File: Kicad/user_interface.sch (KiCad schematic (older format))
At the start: 33 parts, among them SW1 Push, SW10 Push, SW11 Push, SW12 Push, SW13 Rotary_Encoder_Switch, SW14 Rotary_Encoder_Switch, SW15 Rotary_Encoder_Switch, SW2 Push, SW3 Push, SW4 Push, SW5 Push, SW6 Push, SW7 Push, SW8 Push, SW9 Push, U1 TLC59281DBQ

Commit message: completing schematics and starting to correct errors
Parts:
- gave numbers to parts that had none: 17
- renumbered U1 to U3
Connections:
- net GND: now also SW13.C, SW14.C, SW15.C

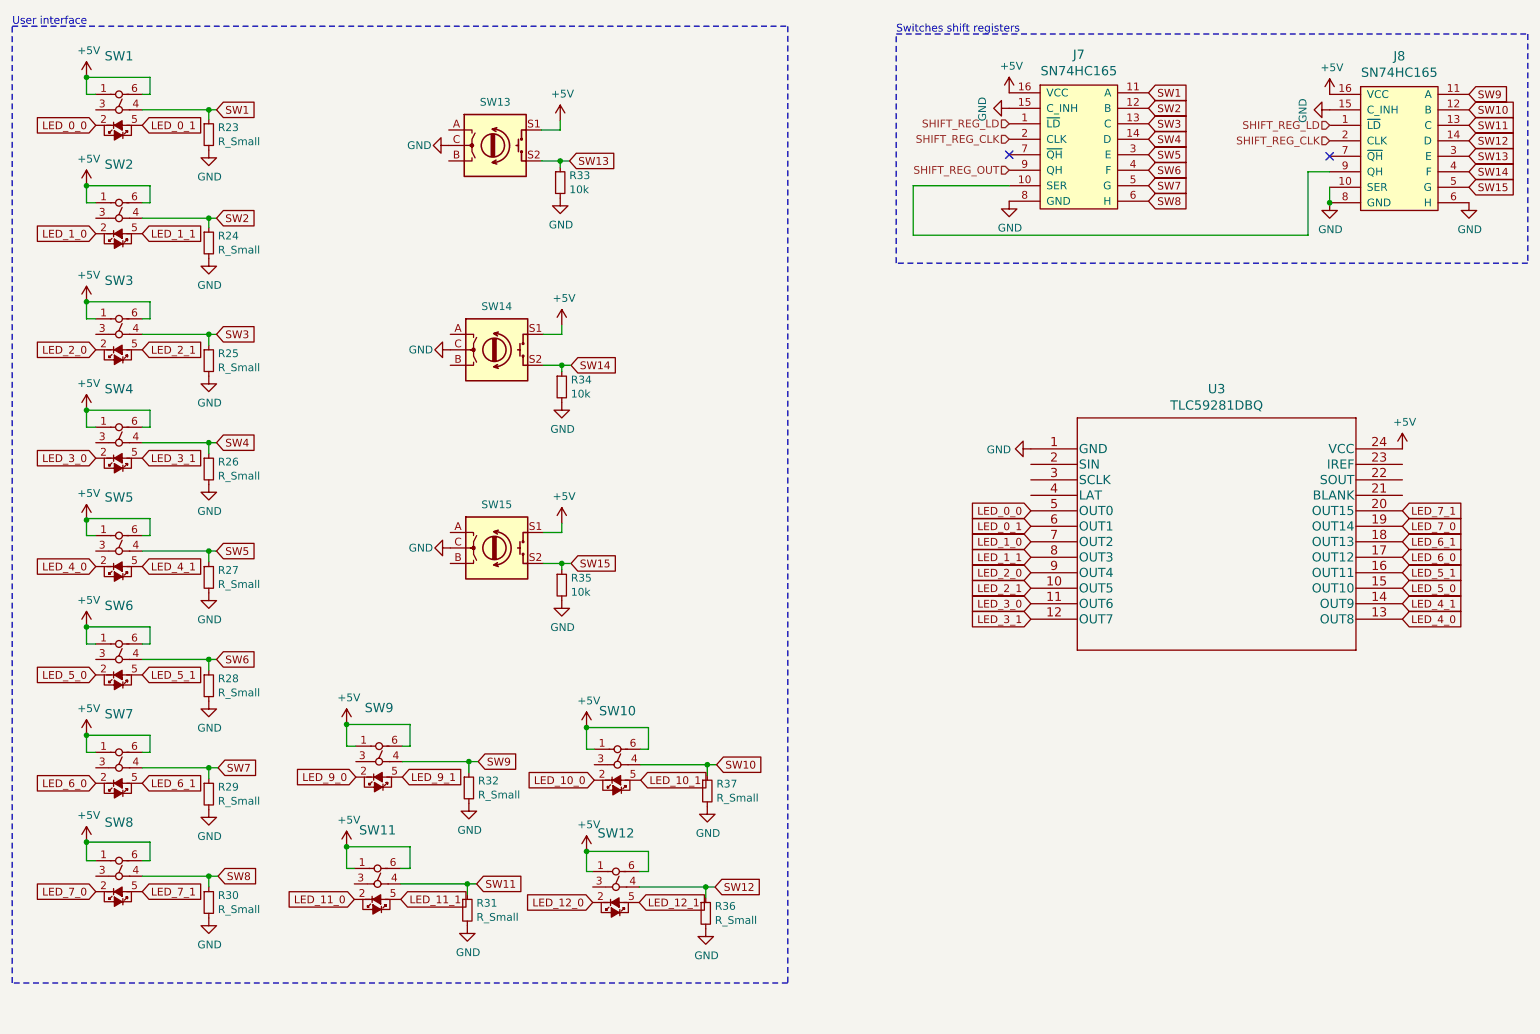
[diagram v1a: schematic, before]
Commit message: correcting some connections
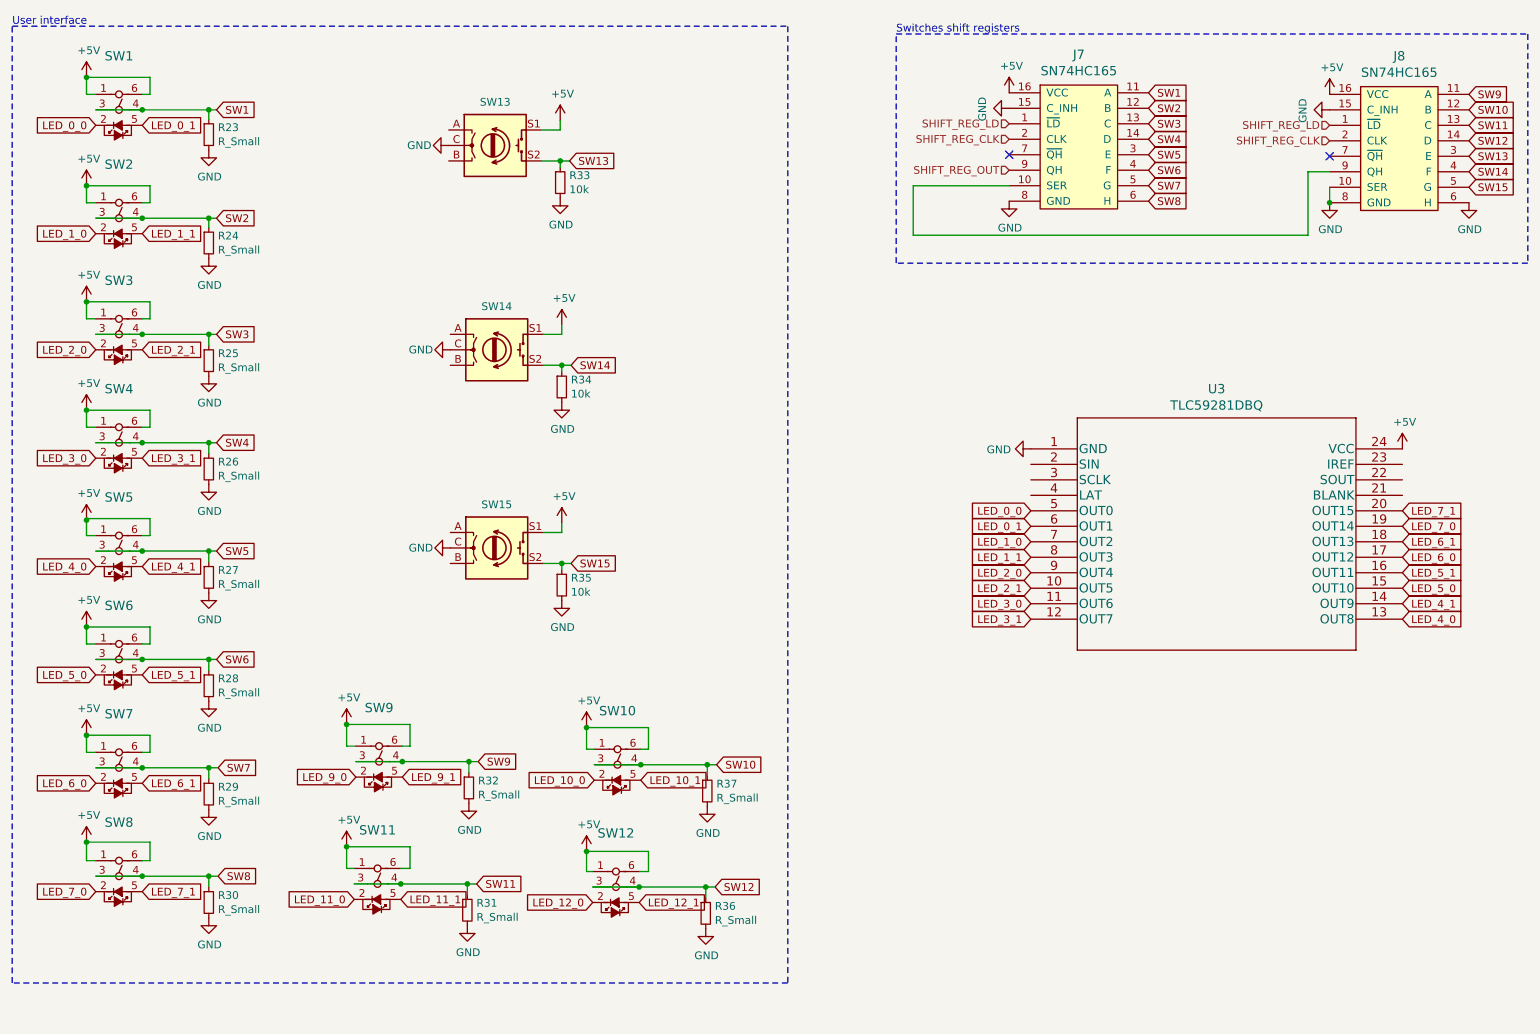
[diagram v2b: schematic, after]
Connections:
- net SW1: now also SW1.3
- net SW10: now also SW10.3
- net SW11: now also SW11.3
- net SW12: now also SW12.3
- net SW2: now also SW2.3
- net SW3: now also SW3.3
- net SW4: now also SW4.3
- net SW5: now also SW5.3
- net SW6: now also SW6.3
- net SW7: now also SW7.3
- net SW8: now also SW8.3
- net SW9: now also SW9.3
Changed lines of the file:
@@
 	0    1    1    0
 $EndComp
+Wire Wire Line
+	1550 1450 1850 1450
+Connection ~ 1850 1450
+Wire Wire Line
+	1550 2150 1850 2150
+Connection ~ 1850 2150
+Wire Wire Line
+	1550 2900 1850 2900
+Connection ~ 1850 2900
+Wire Wire Line
+	1550 3600 1850 3600
+Connection ~ 1850 3600
+Wire Wire Line
+	1550 4300 1850 4300
+Connection ~ 1850 4300
+Wire Wire Line
+	1550 5000 1850 5000
+Connection ~ 1850 5000
+Wire Wire Line
+	1550 5700 1850 5700
+Connection ~ 1850 5700
+Wire Wire Line
+	1550 6400 1850 6400
+Connection ~ 1850 6400
+Wire Wire Line
+	3230 5660 3530 5660
+Connection ~ 3530 5660
+Wire Wire Line
+	3220 6450 3520 6450
+Connection ~ 3520 6450
+Wire Wire Line
+	4770 5680 5070 5680
+Connection ~ 5070 5680
+Wire Wire Line
+	4760 6470 5060 6470
+Connection ~ 5060 6470
 $EndSCHEMATC

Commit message: updated power section with switching regulator
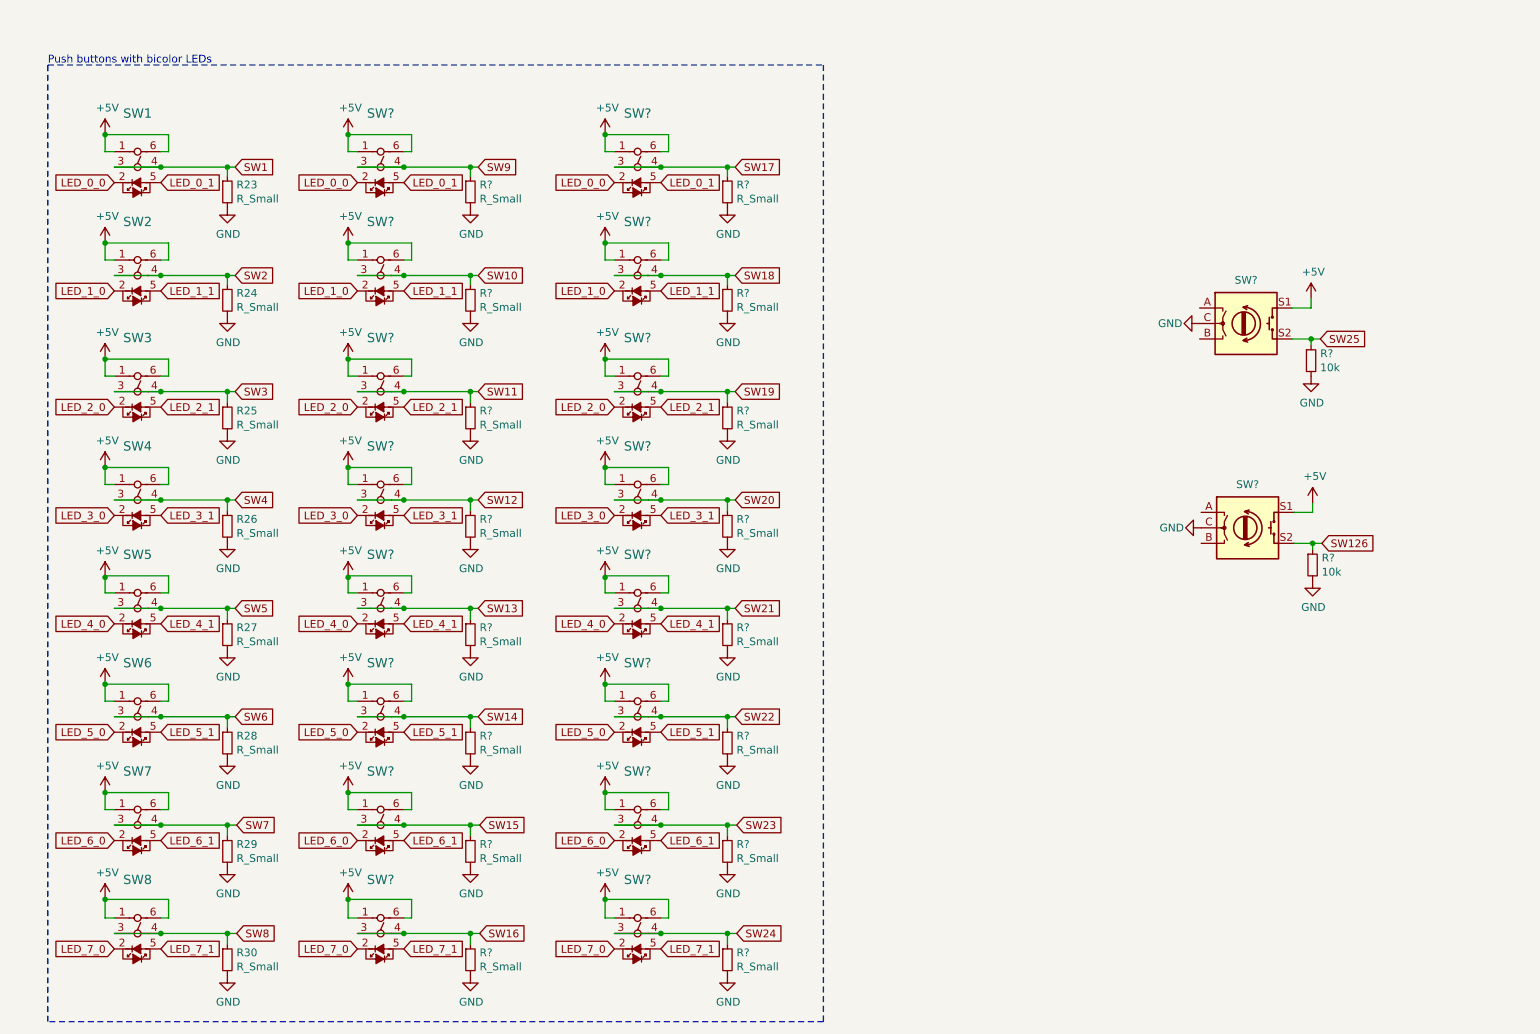
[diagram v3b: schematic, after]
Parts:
- removed J7, J8: SN74HC165, symbol eurocad:SN74HC165
- removed R31, R32, R36, R37: R_Small, symbol Device:R_Small
- removed R33, R34, R35: 10k, symbol Device:R_Small
- removed SW10, SW11, SW12, SW9: Push, footprints:PB614_LED_SW_6pin, symbol sw_push_led_pb614:SW_Push_LED_PB614
- removed SW13, SW14, SW15: Rotary_Encoder_Switch, Rotary_Encoder:RotaryEncoder_Alps_EC12E-Switch_Vertical_H20mm, symbol Device:Rotary_Encoder_Switch
- removed U3: TLC59281DBQ, Package_DFN_QFN:VQFN-24-1EP_4x4mm_P0.5mm_EP2.45x2.45mm, symbol eurorack_custom:ul_TLC59281DBQ_TLC59281DBQ
- added R? (x16): R_Small, symbol Device:R_Small
- added R? (x2): 10k, symbol Device:R_Small
- added SW? (x16): Push, footprints:PB614_LED_SW_6pin, symbol sw_push_led_pb614:SW_Push_LED_PB614
- added SW? (x2): Rotary_Encoder_Switch, Rotary_Encoder:RotaryEncoder_Alps_EC12E-Switch_Vertical_H20mm, symbol Device:Rotary_Encoder_Switch
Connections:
- net +5V: now also SW?.1, SW?.1, SW?.1, SW?.1, SW?.1, SW?.1, SW?.1, SW?.1, SW?.1, SW?.1, SW?.1, SW?.1, SW?.1, SW?.1, SW?.1, SW?.1, SW?.6, SW?.6, SW?.6, SW?.6, SW?.6, SW?.6, SW?.6, SW?.6, SW?.6, SW?.6, SW?.6, SW?.6, SW?.6, SW?.6, SW?.6, SW?.6, SW?.S1, SW?.S1
- net GND: now also R?.2, R?.2, R?.2, R?.2, R?.2, R?.2, R?.2, R?.2, R?.2, R?.2, R?.2, R?.2, R?.2, R?.2, R?.2, R?.2, R?.2, R?.2, SW?.C, SW?.C
- net LED_0_0: now also SW?.2, SW?.2
- net LED_0_1: now also SW?.5, SW?.5
- net LED_1_0: now also SW?.2, SW?.2
- net LED_1_1: now also SW?.5, SW?.5
- net LED_2_0: now also SW?.2, SW?.2
- net LED_2_1: now also SW?.5, SW?.5
- net LED_3_0: now also SW?.2, SW?.2
- net LED_3_1: now also SW?.5, SW?.5
- net LED_4_0: now also SW?.2, SW?.2
- net LED_4_1: now also SW?.5, SW?.5
- net LED_5_0: now also SW?.2, SW?.2
- net LED_5_1: now also SW?.5, SW?.5
- net LED_6_0: now also SW?.2, SW?.2
- net LED_6_1: now also SW?.5, SW?.5
- net LED_7_0: now also SW?.2, SW?.2
- net LED_7_1: now also SW?.5, SW?.5
- net SW10: now also R?.1, SW?.3, SW?.4
- net SW11: now also R?.1, SW?.3, SW?.4
- net SW12: now also R?.1, SW?.3, SW?.4
- net SW13: now also R?.1, SW?.3, SW?.4
- net SW14: now also R?.1, SW?.3, SW?.4
- net SW15: now also R?.1, SW?.3, SW?.4
- net SW9: now also R?.1, SW?.3, SW?.4
- new net SW126: R?.1, SW?.S2
- new net SW16: R?.1, SW?.3, SW?.4
- new net SW17: R?.1, SW?.3, SW?.4
- new net SW18: R?.1, SW?.3, SW?.4
- new net SW19: R?.1, SW?.3, SW?.4
- new net SW20: R?.1, SW?.3, SW?.4
- new net SW21: R?.1, SW?.3, SW?.4
- new net SW22: R?.1, SW?.3, SW?.4
- new net SW23: R?.1, SW?.3, SW?.4
- new net SW24: R?.1, SW?.3, SW?.4
- new net SW25: R?.1, SW?.S2
- no-connect marks 2 -> 0
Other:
- note added: "Push buttons with bicolor LEDs"
- note removed: "Switches shift registers"
- note removed: "User interface"
- moved on the sheet: R23, R24, R25, R26, R27, R28, R29, R30, SW1, SW2, SW3, SW4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
